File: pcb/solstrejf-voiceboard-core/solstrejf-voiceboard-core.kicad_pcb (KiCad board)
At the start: 2 copper layers, 119.4 x 83.8 mm, 128 parts, among them J1 PSU+Power Connector, J2 Mod-Matrix Connector, J3 Direct_Out, J4 Front Panel Connector, U1 AS3372E, U2 L78L05, U3 L79L05, U4 TL072, U5 LM324, U6 ONESHOT, U7 L78L12, U8 L79L12

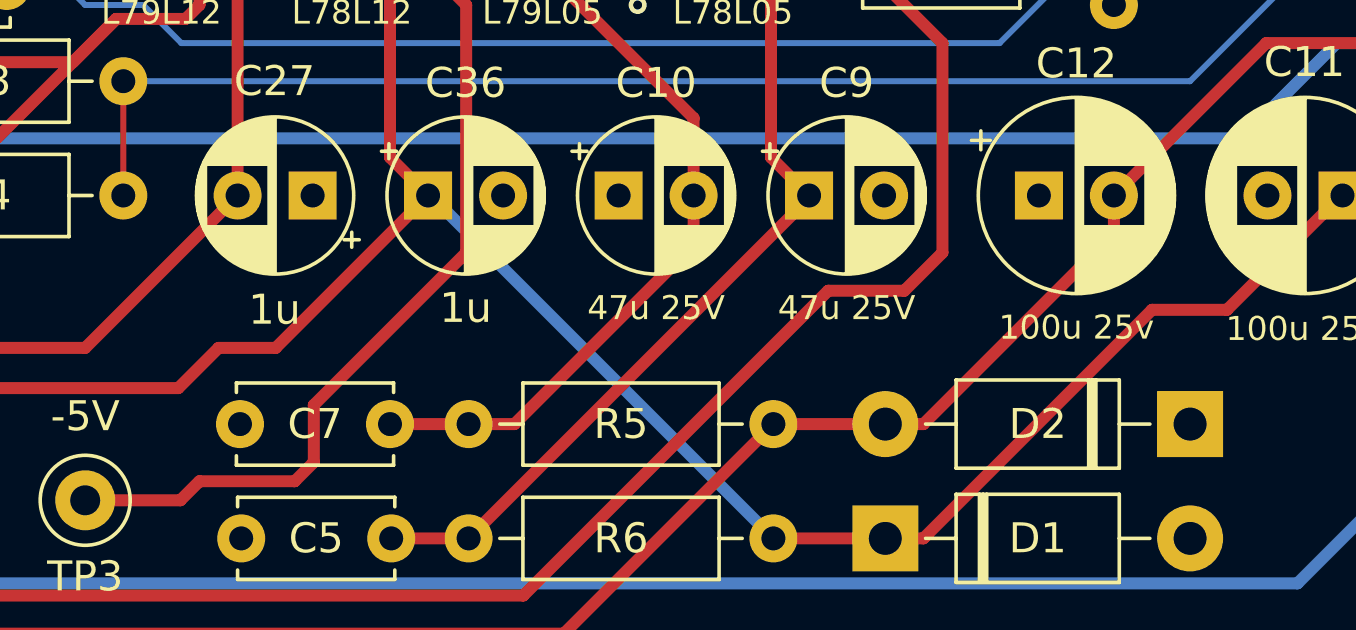
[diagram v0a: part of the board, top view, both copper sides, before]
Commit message: Updated values of electrolytic caps on voice board to match in the ibom.
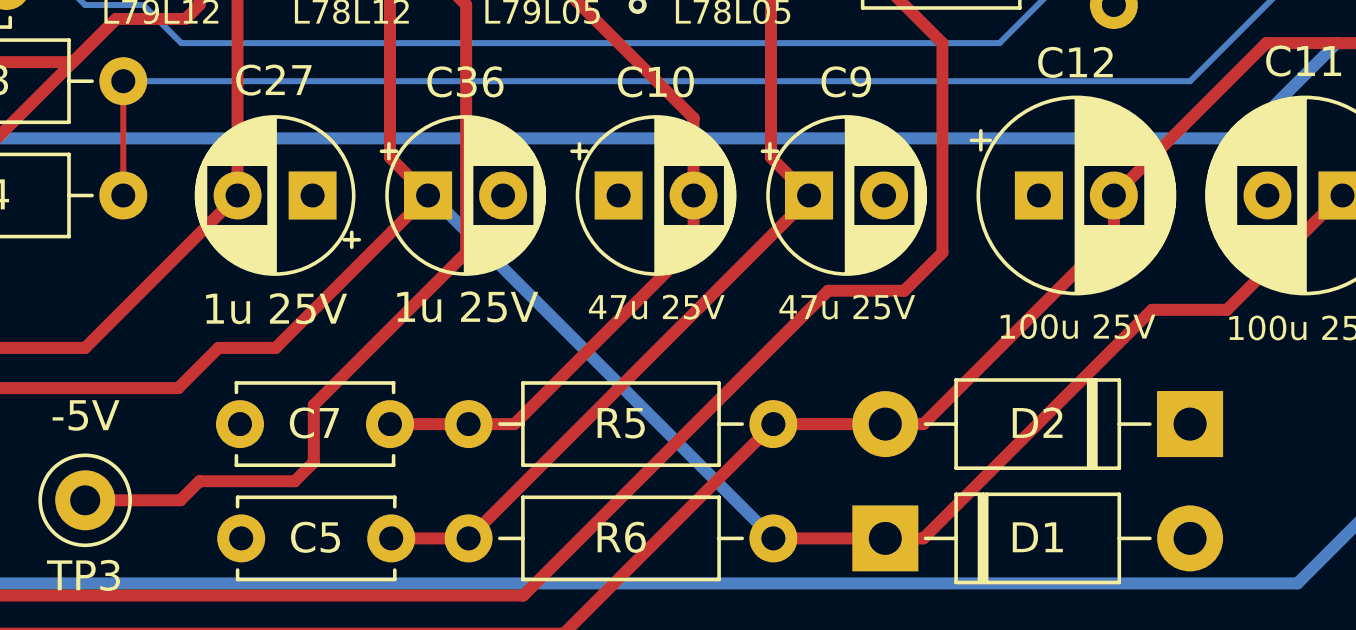
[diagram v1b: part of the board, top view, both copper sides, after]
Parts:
- C12: value 100u 25v -> 100u 25V
- C27, C36: value 1u -> 1u 25V
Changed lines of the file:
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@@
 			)
 		)
-		(property "Value" "1u"
+		(property "Value" "1u 25V"
 			(at 1.25 3.75 0)
 			(layer "F.SilkS")
@@
 			)
 		)
-		(property "Value" "1u"
+		(property "Value" "1u 25V"
 			(at 1.27 -3.81 0)
 			(layer "F.SilkS")
@@
 			)
 		)
-		(property "Value" "100u 25v"
+		(property "Value" "100u 25V"
 			(at 1.25 4.4 0)
 			(layer "F.SilkS")

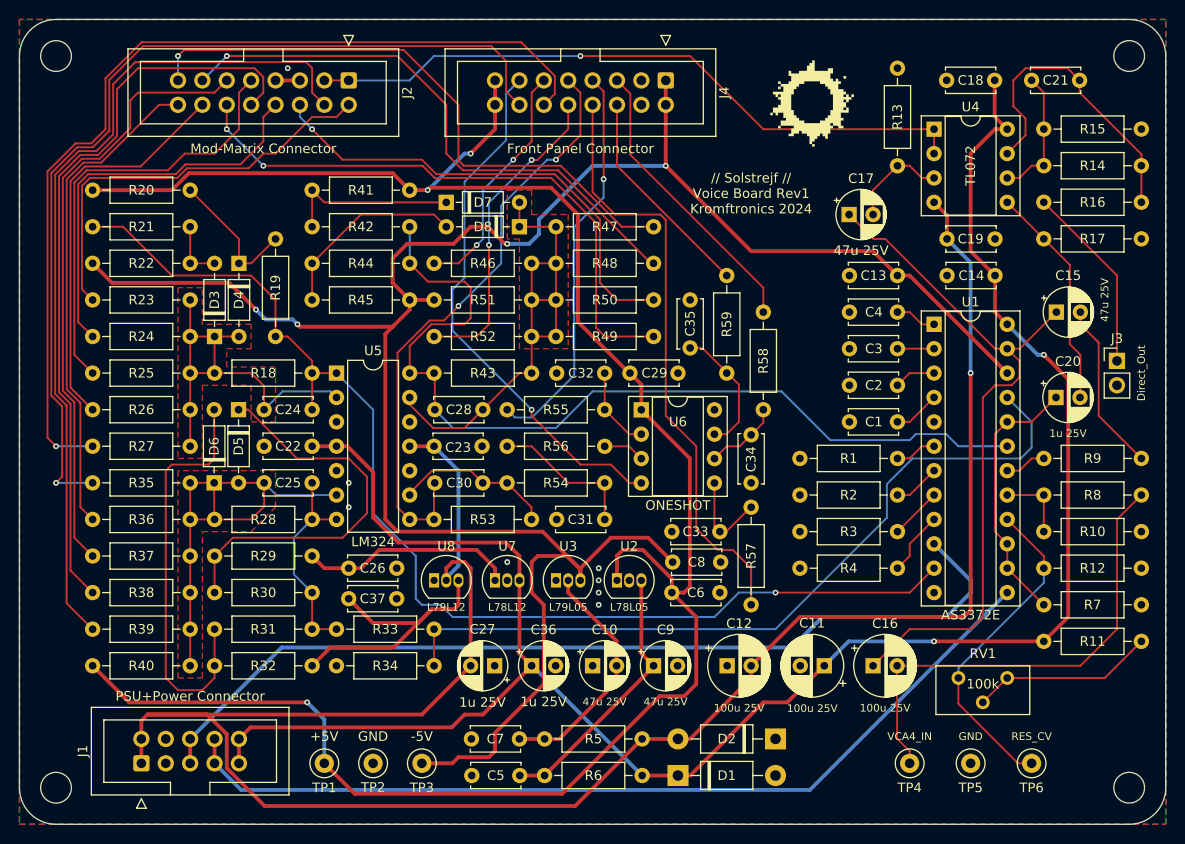
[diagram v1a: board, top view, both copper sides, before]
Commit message: Added variable revision and date silkscreen prints for all four boards of Solstrejf
This means that the revision and issue date that is set in the page setup
of the PCB's will be update on the silscreen automatically so I don't forget
to update the revsions on the silkscreen :')
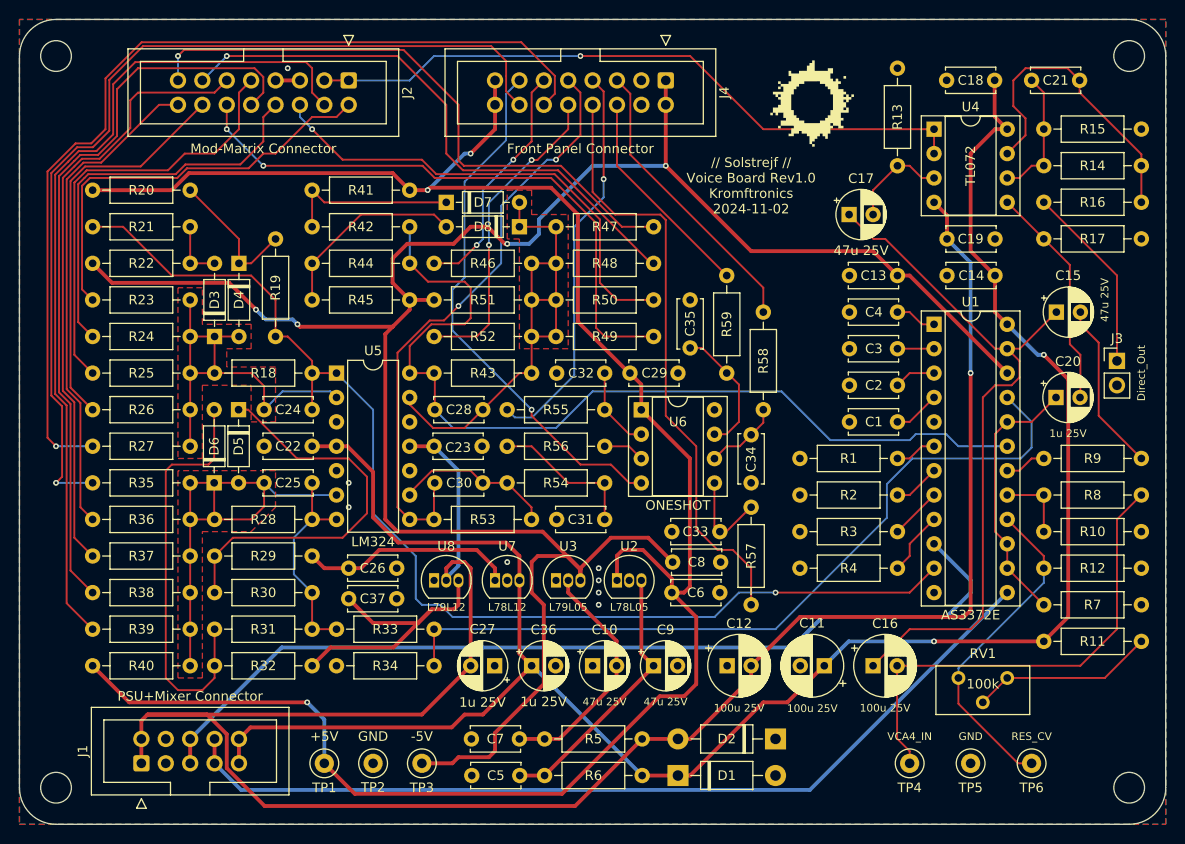
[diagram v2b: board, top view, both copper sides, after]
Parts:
- J1: value PSU+Power Connector -> PSU+Mixer Connector
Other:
- board text added: "// Solstrejf // Voice Board Rev${REVISION} ${COMPANY} ${ISSUE_DATE}"
- board text removed: "// Solstrejf // Voice Board Rev1 Kromftronics 2024"
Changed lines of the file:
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@@
 		(date "2024-11-02")
 		(rev "1.0")
+		(company "Kromftronics")
 	)
 	(layers
@@
 			)
 		)
-		(property "Value" "PSU+Power Connector"
+		(property "Value" "PSU+Mixer Connector"
 			(at 6.985 5.08 0)
 			(layer "F.SilkS")
@@
 		(layer "Edge.Cuts")
 	)
-	(gr_text "// Solstrejf // \nVoice Board Rev1\nKromftronics 2024"
+	(gr_text "// Solstrejf // \nVoice Board Rev${REVISION}\n${COMPANY}\n${ISSUE_DATE}"
 		(at 156.21 77.47 0)
 		(layer "F.SilkS")

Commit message: Created rev1.1 of Solstref voice board. Updated value of some resistors (66k->68k). Exported new ibom and schematic.
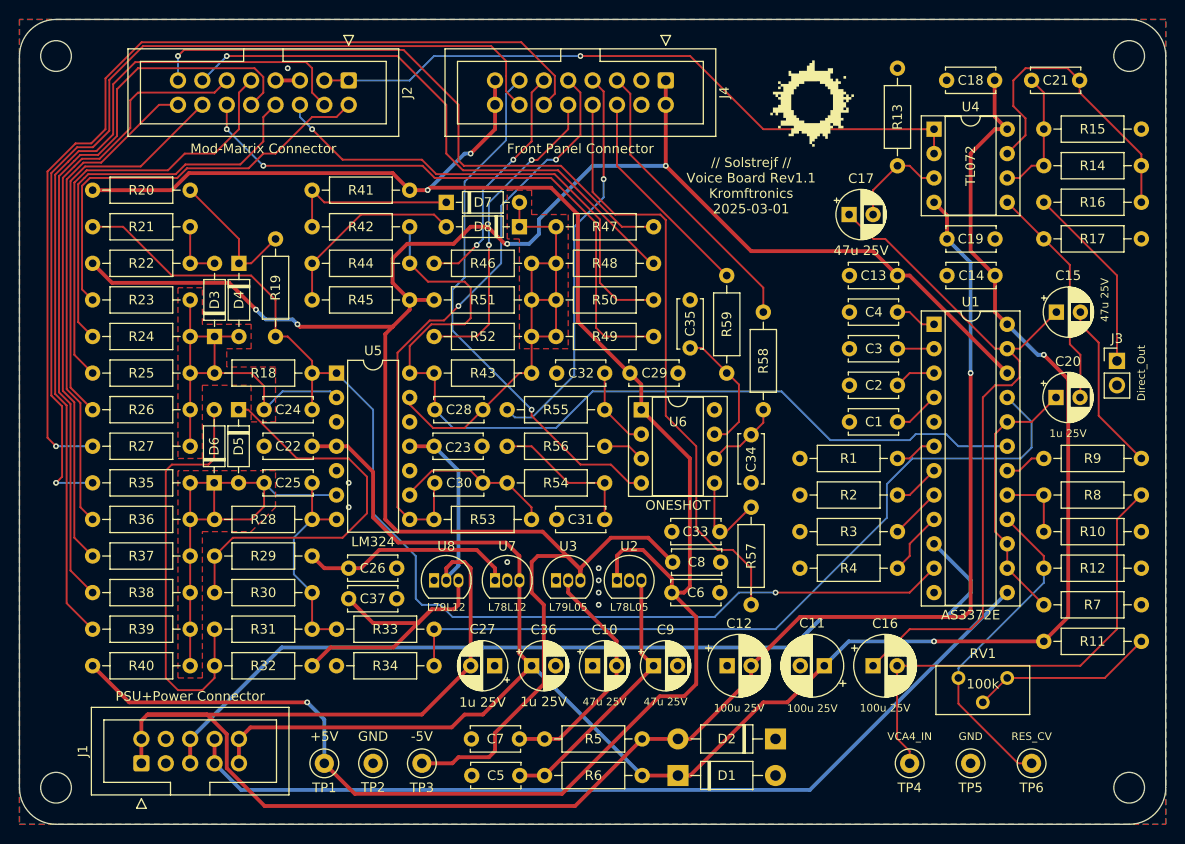
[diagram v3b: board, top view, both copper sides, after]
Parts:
- J1: value PSU+Mixer Connector -> PSU+Power Connector
- R36, R37, R38, R39: value 66k -> 68k

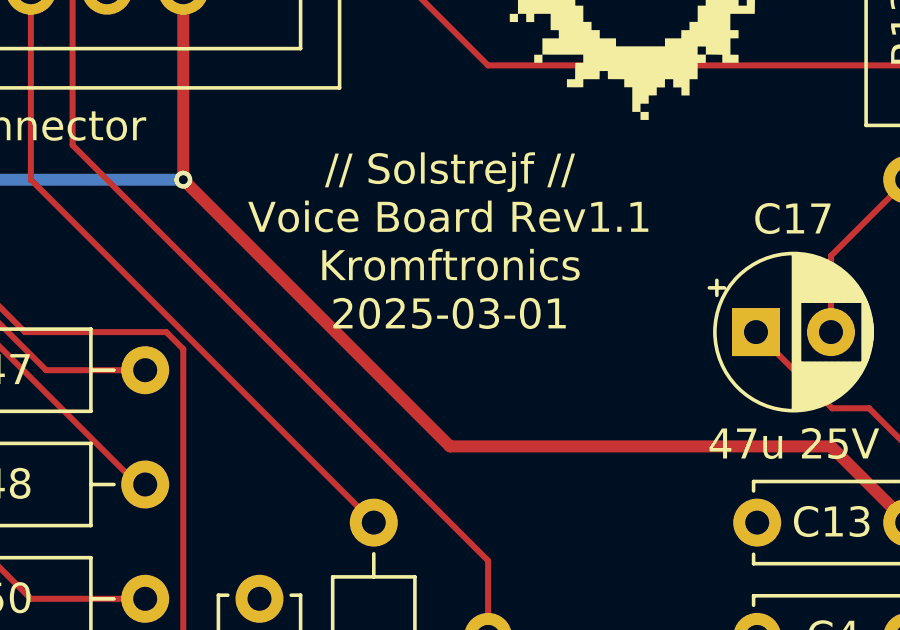
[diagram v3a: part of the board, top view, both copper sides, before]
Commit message: Updated resistor value in VCF CV circuit. Generated new ibom and schematic.
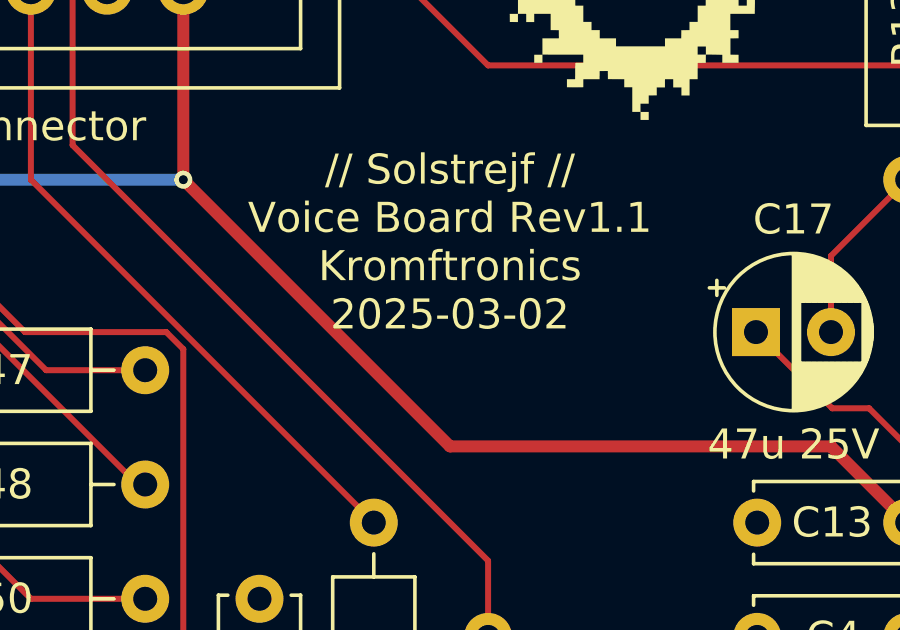
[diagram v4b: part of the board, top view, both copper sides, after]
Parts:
- R35: value 14k -> 15k
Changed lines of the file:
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@@
 	(title_block
 		(title "Solstrejf Voice Board")
-		(date "2025-03-01")
+		(date "2025-03-02")
 		(rev "1.1")
 		(company "Kromftronics")
@@
 			)
 		)
-		(property "Value" "14k"
+		(property "Value" "15k"
 			(at 5.08 0 0)
 			(layer "F.SilkS")

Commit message: Updated two capacitor values in voice board power section 330n->100n. Updated Schematic and created new IBOM.
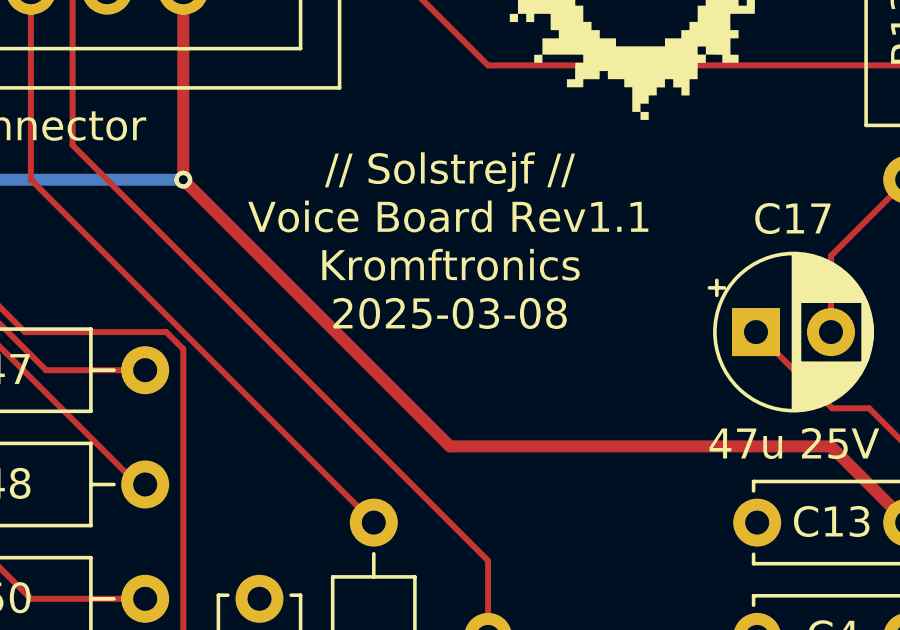
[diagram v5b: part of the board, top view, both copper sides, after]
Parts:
- C5, C7: value 330n -> 100n
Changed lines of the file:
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@@
 	(title_block
 		(title "Solstrejf Voice Board")
-		(date "2025-03-02")
+		(date "2025-03-08")
 		(rev "1.1")
 		(company "Kromftronics")
@@
 			)
 		)
-		(property "Value" "330n"
+		(property "Value" "100n"
 			(at 2.54 0 0)
 			(layer "F.SilkS")
@@
 			)
 		)
-		(property "Value" "330n"
+		(property "Value" "100n"
 			(at 2.54 0 0)
 			(layer "F.SilkS")
